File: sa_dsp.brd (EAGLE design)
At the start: 150 x 110 mm, 327 parts, among them CN1 uSD, CN3 2X5 HEADER, Q3 2N7002, Q4 2N7002, SW1 1825910-7, U1 PGA2311, U10 LME49720, U11 PGA2311, U12 LME49720, U13 LME49720, U14 PCM1754, U15 LME49720, U16 PGA2311, U17 LME49720, U18 LME49720, U19 PCM1754, U2 LM317, U20 LME49720, U21 7 SEG, U22 74HC164A, U23 PCM2707, U24 PCM2707, U25 7 SEG, U26 74HC164A, U27 LM337, U28 LM317, U29 7 SEG, U3 OSD3358-512M-BSM, U30 74HC164A, U31 100MHz, U4 LME49720, U5 LME49720, U6 10CL016YF484C6G, U7 7 SEG, U8 74HC164A, U9 PCM1754

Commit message: DSP progress
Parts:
- added C133: 2.2uF 25V, CAPACITORS:0603
- added C134, C138: 100pF 50V, CAPACITORS:0603
- added C135, C136, C137, C139: 100nF 16V, CAPACITORS:0603
- added CN2, CN4: MINI B USB, CONNECTORs:MUSB-05-S-B-SM-A
- added FB17, FB6: 600R, INDUCTORS:0603
- added TP3, TP4, TP5, TP6, TP7: 2MM_TEST_POINT, MISC:2MM_TEST_PAD
- added U32, U34: USBLC6-2SC6, ICs:SOT23-6
- added U33: FT230X, ICs:SSOP16-4MM
- moved CN3 44.7 mm to (99.8, 74.9), turned to 180 degrees
- moved R85 40.4 mm to (96.0, 79.1), turned to 270 degrees
- moved R14 40.3 mm to (96.5, 76.1), turned to 270 degrees
- moved R86 40.0 mm to (96.2, 69.1), turned to 270 degrees
- moved R87 39.7 mm to (96.2, 72.6), turned to 270 degrees
- moved R15 37.4 mm to (94.5, 75.1), turned to 270 degrees
- moved R84 36.9 mm to (93.6, 78.6), turned to 270 degrees
- moved C123 13.2 mm to (46.8, 46.5), turned to 270 degrees
- moved C122 12.8 mm to (52.5, 47.0), turned to 90 degrees
- moved XTAL4 12.3 mm to (49.6, 46.8), turned to 0 degrees
- moved Q3 9.45 mm to (31.9, 40.0)
- moved Q4 9.45 mm to (35.4, 40.0)
- moved R72 9.45 mm to (35.8, 37.6)
- moved R73 9.45 mm to (35.8, 42.4)
- moved D6 9.13 mm to (52.5, 100.0), turned to 180 degrees
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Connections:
- removed net AM_STM_NRST: U3.P5
- removed net STM32_BOOT0: U3.R5
- new net AM_I2C0_SCL: TP3.1, U3.C10, U3.D10
- new net AM_I2C0_SDA: TP4.1, U3.C11, U3.D11
- new net FT_DB_3V3: C133.2, C137.2, U33.10, U33.11, U33.3, U33.6
- new net FT_DB_USB_5V: C134.2, C135.2, C136.2, FB6.2, U32.5, U33.12
- new net N$183: CN2.D-, U32.6
- new net N$199: CN2.D+, U32.4
- new net N$200: U32.1, U33.9
- new net N$201: U32.3, U33.8
- new net N$202: CN2.VCC, FB6.1
- new net N$203: CN4.VCC, FB17.1
- new net OSD_SPI_CS_FPGA: U3.A14
- new net OSD_SPI_MISO: U3.B14
- new net OSD_SPI_MOSI: U3.B13
- new net OSD_SPI_SCLK: U3.A13
- net 5VUSB: now also C138.2, C139.2, FB17.2, U34.5
- net AM_DEBUG_UART_RX: now also U33.4
- net AM_DEBUG_UART_TX: now also U33.1
- net AM_EEPROM_WP: now also TP5.1
- net AM_WARM_!RST: now also TP7.1
- net GND: now also C133.1, C134.1, C135.1, C136.1, C137.1, C138.1, C139.1, CN2.GND, CN2.SHIELD1, CN2.SHIELD2, CN2.SHIELD3, CN2.SHIELD4, CN4.GND, CN4.SHIELD1, CN4.SHIELD2, CN4.SHIELD3, CN4.SHIELD4, TP6.1, U32.2, U33.13, U33.5, U34.2
- net N$134: now also CN4.D-, U34.4; no longer U3.C10, U3.D10
- net N$135: now also CN4.D+, U34.6; no longer U3.C11, U3.D11
- net N$172: now also R103.1, U34.3; no longer R102.1
- net N$173: now also R102.1, U34.1; no longer R103.1
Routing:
- net AM_DEBUG_UART_TX: track 0.00 -> 99.7 mm
- net AM_DEBUG_UART_RX: track 0.00 -> 98.0 mm
- net UI_INPUT_SEL: track 0.00 -> 88.6 mm
- net UI_INPUT_AIRPLAY: track 0.00 -> 74.5 mm
- net OSD_SPI_SCLK: track 0.00 -> 56.0 mm, vias 0 -> 1
- net OSD_SPI_MOSI: track 0.00 -> 55.0 mm, vias 0 -> 1
- net OSD_SPI_CS_FPGA: track 0.00 -> 54.5 mm, vias 0 -> 1
- net OSD_SPI_MISO: track 0.00 -> 53.9 mm, vias 0 -> 1
- net UI_INPUT_USB: track 0.00 -> 52.4 mm
- net 5VUSB: track 10.5 -> 48.8 mm
- net PCM_I2S_BCLK_EXT: track 0.00 -> 36.5 mm, vias 0 -> 1
- net PCM_I2S_MCLK_EXT: track 0.00 -> 36.0 mm, vias 0 -> 1
- net PCM_I2S_DOUT_EXT: track 0.00 -> 35.7 mm, vias 0 -> 1
- net AM_USR_LED3: track 6.61 -> 39.6 mm
- net PCM_I2S_LRCLK_EXT: track 0.00 -> 29.4 mm, vias 0 -> 1
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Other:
- board text added: "APL"
- board text added: "USB"

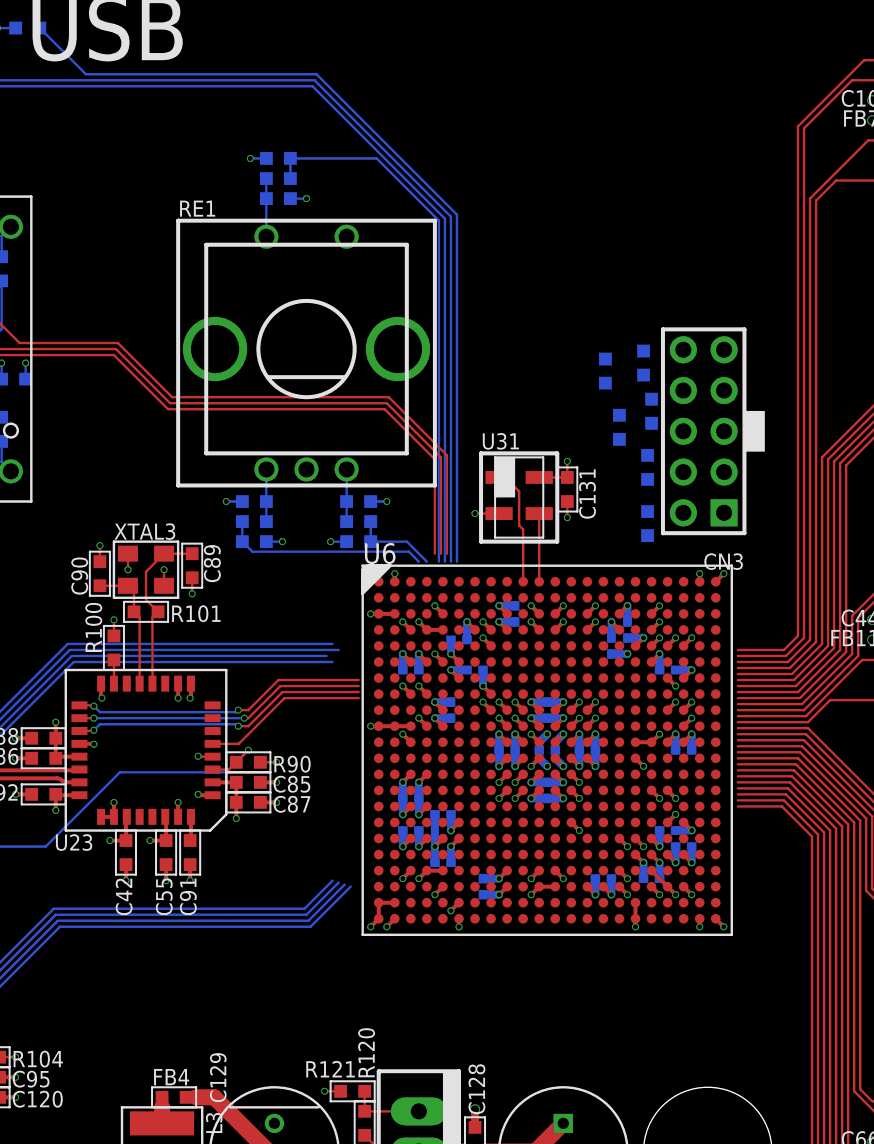
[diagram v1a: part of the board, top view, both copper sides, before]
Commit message: Added female USB
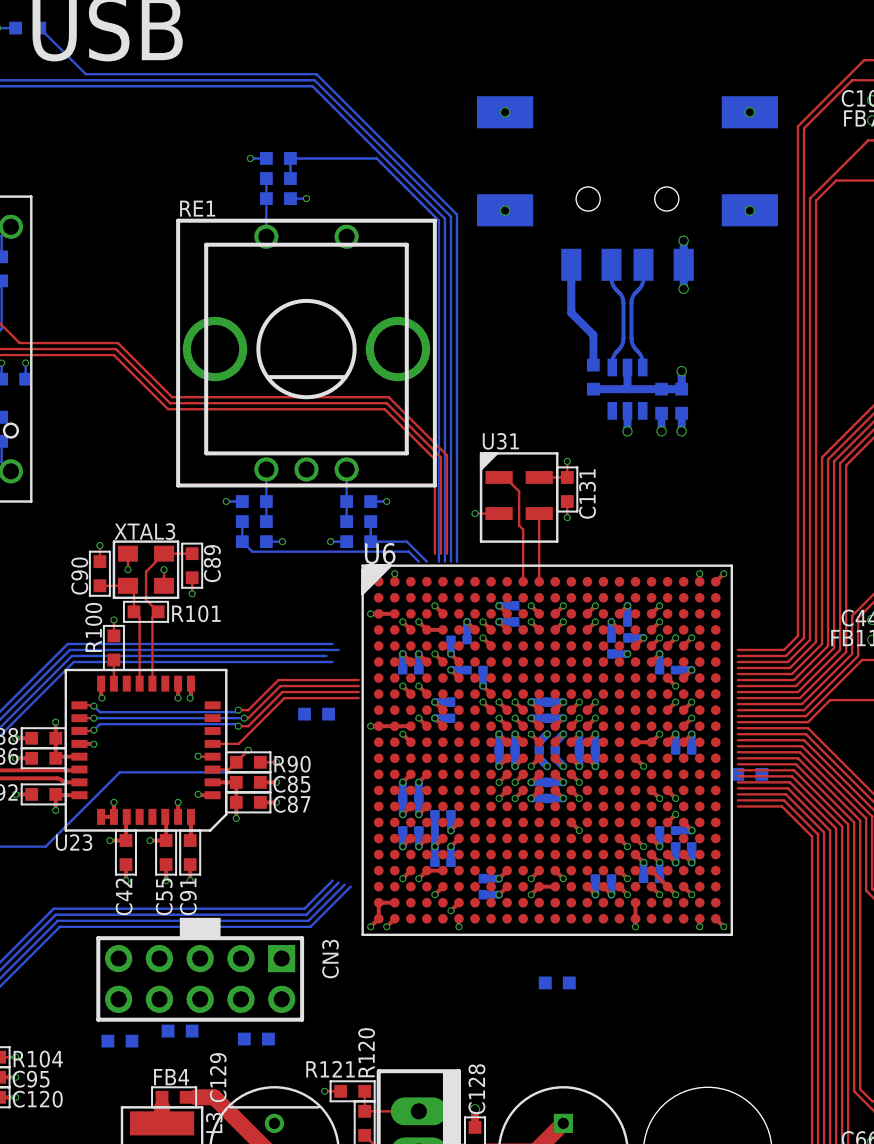
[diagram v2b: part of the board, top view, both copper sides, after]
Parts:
- added C140: 100pF 50V, CAPACITORS:0603
- added C141: 100nF 16V, CAPACITORS:0603
- added CN5: USB A, CONNECTORs:629104190121
- added FB18: 600R, INDUCTORS:0603
- added U35: USBLC6-2SC6, ICs:SOT23-6
- moved R84 51.6 mm to (63.4, 36.9), turned to 180 degrees
- moved R14 48.5 mm to (67.1, 37.5), turned to 180 degrees
- moved CN3 46.4 mm to (68.4, 40.8), turned to 270 degrees
- moved R15 44.3 mm to (71.9, 37.0), turned to 180 degrees
- moved R87 32.6 mm to (90.6, 40.5), turned to 180 degrees
- moved R85 29.9 mm to (75.6, 57.2), turned to 0 degrees
- moved R86 16.9 mm to (102.6, 53.5), turned to 180 degrees
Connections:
- new net N$204: CN5.2, U35.4
- new net N$205: CN5.3, U35.6
- new net N$206: CN5.1, FB18.1
- new net WIFI_USB_D+: U35.1
- new net WIFI_USB_D-: U35.3
- net 5VD: now also C140.2, C141.2, FB18.2, U35.5
- net GND: now also C140.1, C141.1, CN5.4, CN5.SH1, CN5.SH2, CN5.SH3, CN5.SH4, U35.2
- net OSD_SPI_MISO: now also U3.B13; no longer U3.B14
- net OSD_SPI_MOSI: now also U3.B14; no longer U3.B13
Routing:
- net 5VD: track 27.9 -> 35.9 mm, vias 3 -> 4
- net N$206: track 0.00 -> 6.82 mm
- net N$205: track 0.00 -> 6.76 mm
- net N$204: track 0.00 -> 6.76 mm
- net GND: track 245.7 -> 252.3 mm, vias 235 -> 244
- net OSD_SPI_MOSI: track 55.0 -> 53.9 mm
- net OSD_SPI_MISO: track 53.9 -> 55.0 mm

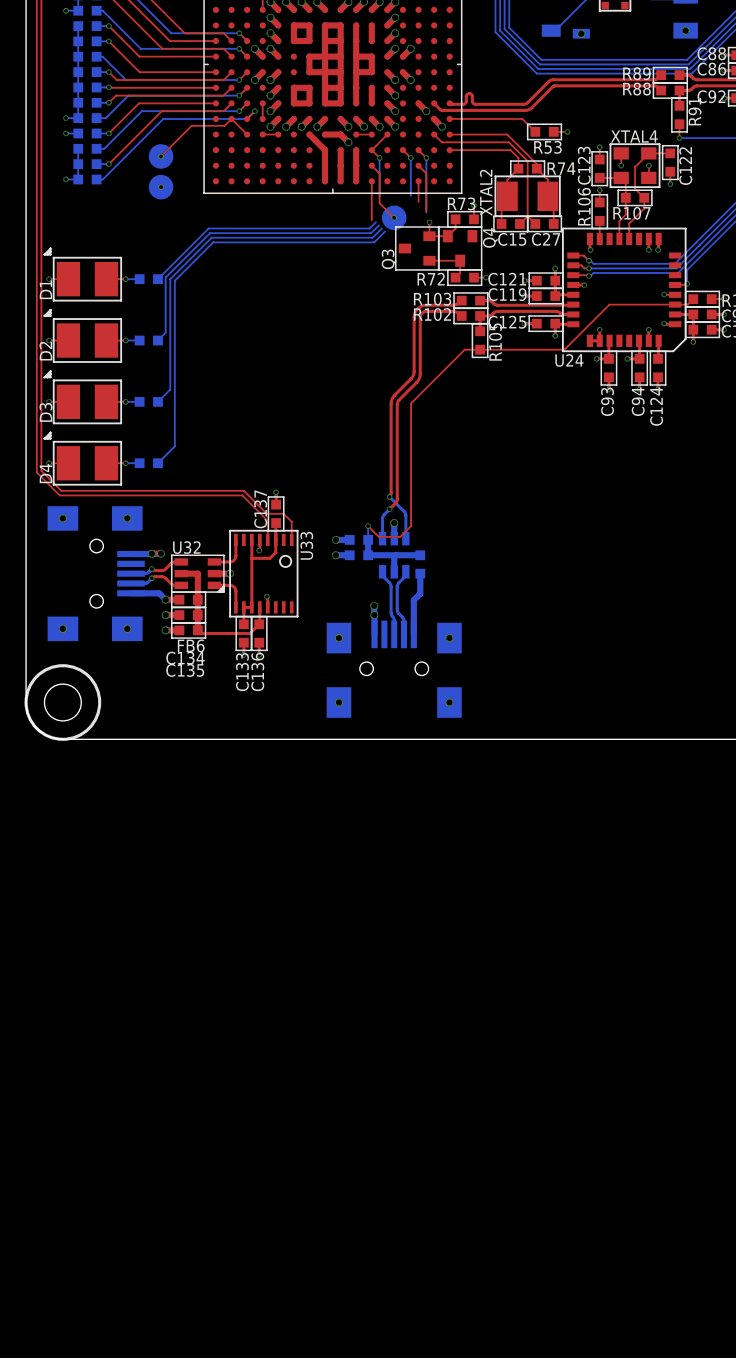
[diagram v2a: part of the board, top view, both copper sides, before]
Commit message: USB hub added
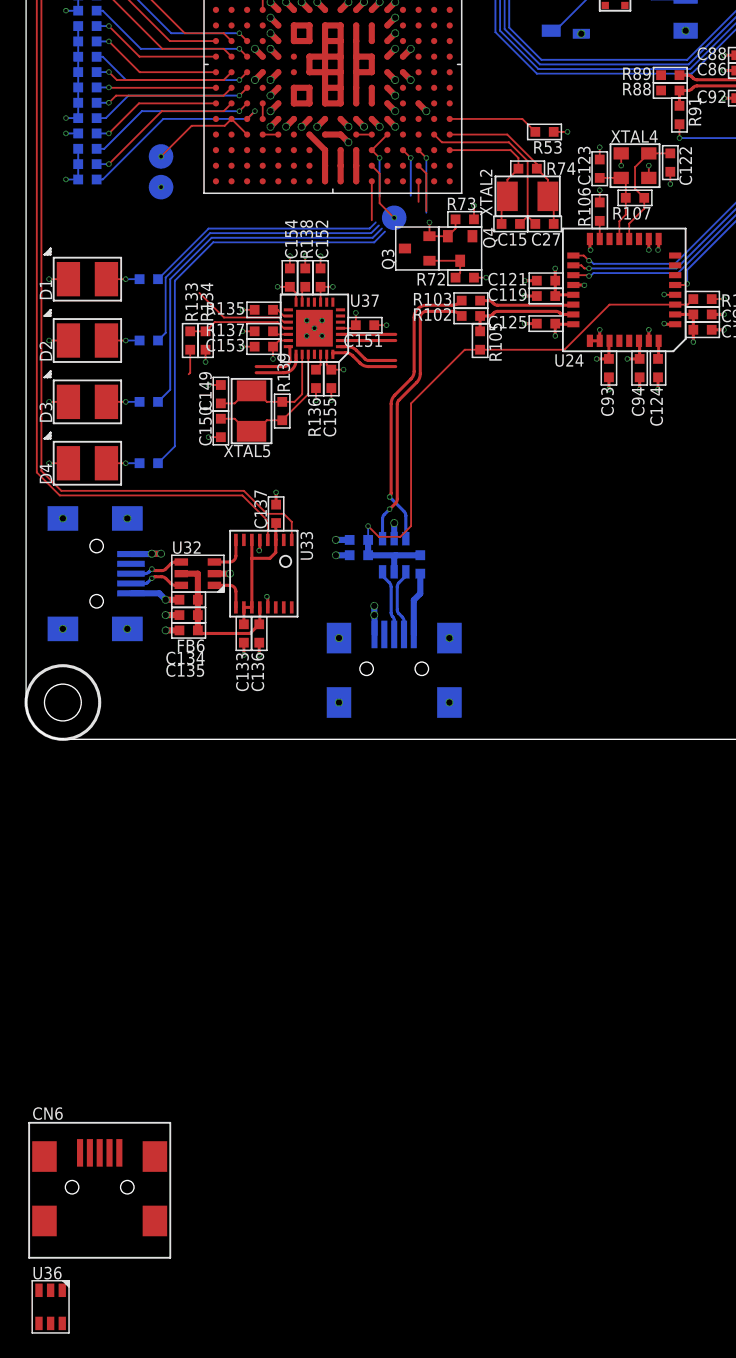
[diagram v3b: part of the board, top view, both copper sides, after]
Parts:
- added C149, C150: 10pF 100V, CAPACITORS:0603
- added C151, C152, C153, C154, C155: 100nF 16V, CAPACITORS:0603
- added CN6: MINI B USB, CONNECTORs:MUSB-05-S-B-SM-A
- added R133: 10k, r_0603:0603
- added R134: 20k, r_0603:0603
- added R135, R137, R138: 51k, r_0603:0603
- added R136: 12k, r_0603:0603
- added R139: 1.0M, r_0603:0603
- added U36: USBLC6-2SC6, ICs:SOT23-6
- added U37: 2 PORT HUB, ICs:QFN28-3.1EPAD
- added XTAL5: 24MHz, CRYSTALS:5X3.2SMD
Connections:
- removed net WIFI_USB_D+: U35.1
- removed net WIFI_USB_D-: U35.3
- new net N$207: U3.M14, U3.M15
- new net N$208: CN6.D+, U36.6
- new net N$209: CN6.D-, U36.4
- new net N$229: R133.2, R134.2, U37.18
- new net N$230: R135.2, U37.16
- new net N$231: R136.2, U37.26
- new net N$232: R138.2, U37.13
- new net N$233: R137.2, U37.19
- new net N$234: C150.2, R139.2, U37.24, XTAL5.1
- new net N$235: C149.2, R139.1, U37.23, XTAL5.2
- new net OSD_DEBUG_USB_DM: U3.K16, U36.3
- new net OSD_DEBUG_USB_DP: U3.K15, U36.1
- new net OSD_DEBUG_USB_ID: CN6.ID, U3.K14
- new net USB_OUT0_DN: U35.3, U37.28
- new net USB_OUT0_DP: U35.1, U37.1
- new net USB_OUT1_DN: R89.1, U37.2
- new net USB_OUT1_DP: R88.1, U37.3
- new net USB_RESET: U37.17
- net 3V3: now also C151.2, C152.2, C153.2, C154.2, C155.2, U37.10, U37.14, U37.20, U37.27, U37.4
- net 5VD: now also U3.J16; no longer U3.M15
- net 5VUSB: now also R133.1
- net GND: now also C149.1, C150.1, C151.1, C152.1, C153.1, C154.1, C155.1, CN6.GND, CN6.SHIELD1, CN6.SHIELD2, CN6.SHIELD3, CN6.SHIELD4, R134.1, R135.1, R136.1, R137.1, R138.1, U36.2, U37.PAD
- net OSD_USB1_DM: now also U37.21; no longer R89.1
- net OSD_USB1_DP: now also U37.22; no longer R88.1
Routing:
- net OSD_USB1_DP: track 19.6 -> 4.16 mm
- net OSD_USB1_DM: track 19.3 -> 4.21 mm
- net N$234: track 0.00 -> 12.1 mm
- net GND: track 252.3 -> 264.3 mm, vias 244 -> 261
- net 3V3: track 106.3 -> 118.3 mm, vias 67 -> 72
- net N$235: track 0.00 -> 10.9 mm
- net N$229: track 0.00 -> 8.52 mm
- net USB_RESET: track 0.00 -> 8.23 mm
- net USB_OUT0_DN: track 0.00 -> 5.60 mm
- net USB_OUT0_DP: track 0.00 -> 4.88 mm
- net USB_OUT1_DP: track 0.00 -> 4.50 mm
- net USB_OUT1_DN: track 0.00 -> 4.50 mm
- net 5VUSB: track 48.8 -> 50.8 mm
- net N$230: track 0.00 -> 1.46 mm
- net N$231: track 0.00 -> 1.41 mm
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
